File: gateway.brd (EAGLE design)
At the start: 100 x 146 mm, 25 parts, among them J1 RASPBERRYPI-40-PIN-GPIO_PTH_N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, Q1 BSS123

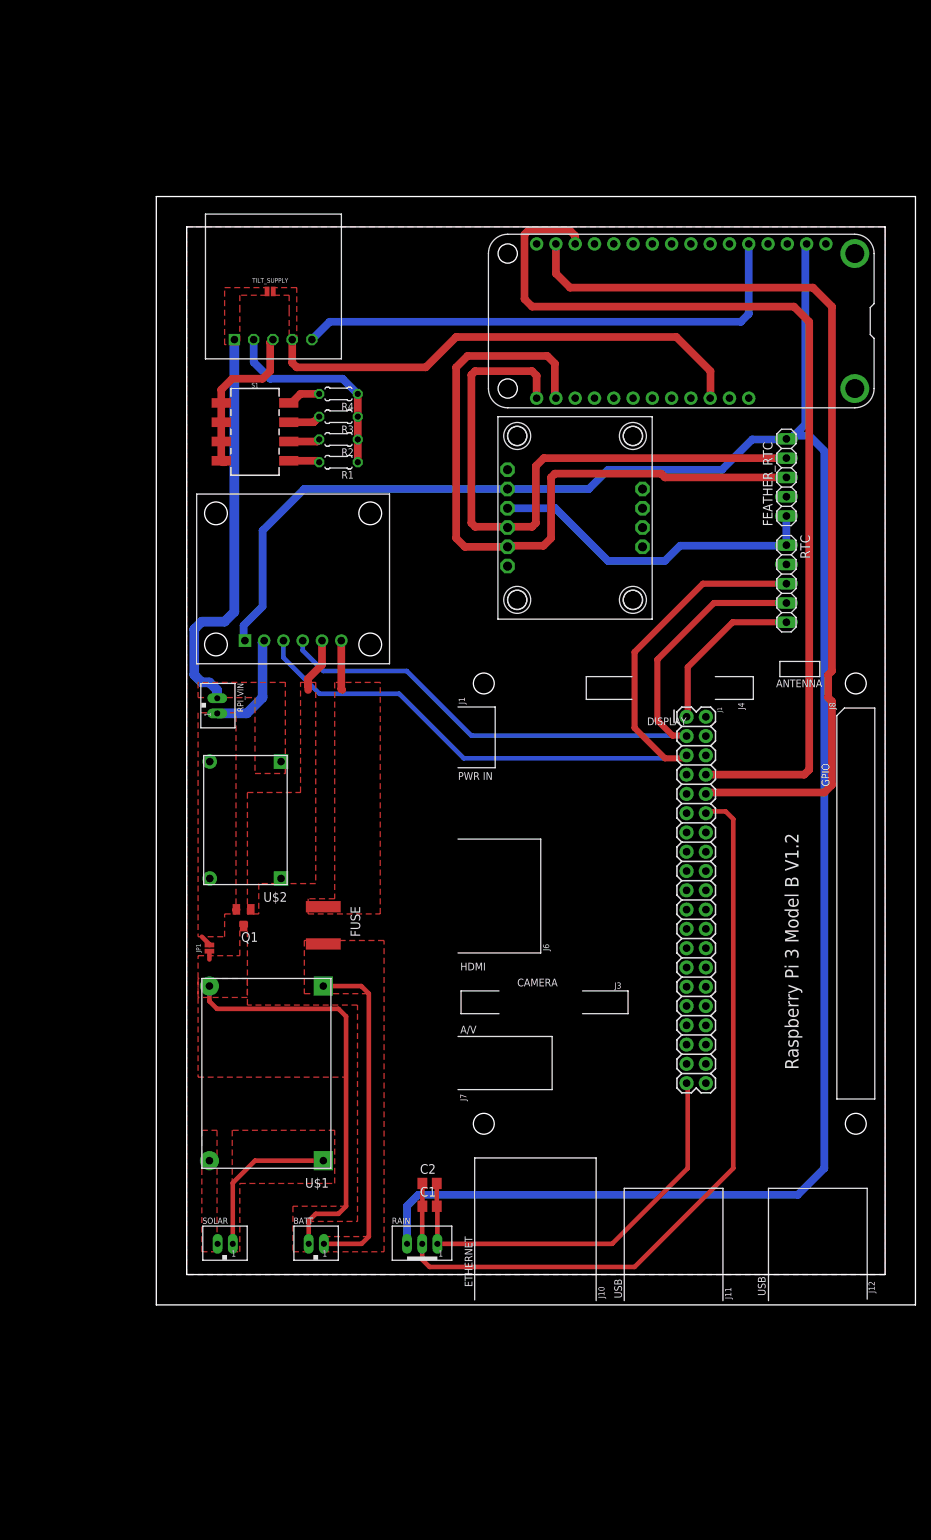
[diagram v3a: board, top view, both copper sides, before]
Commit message: added pads to the microcontrollers ( feather and pi )
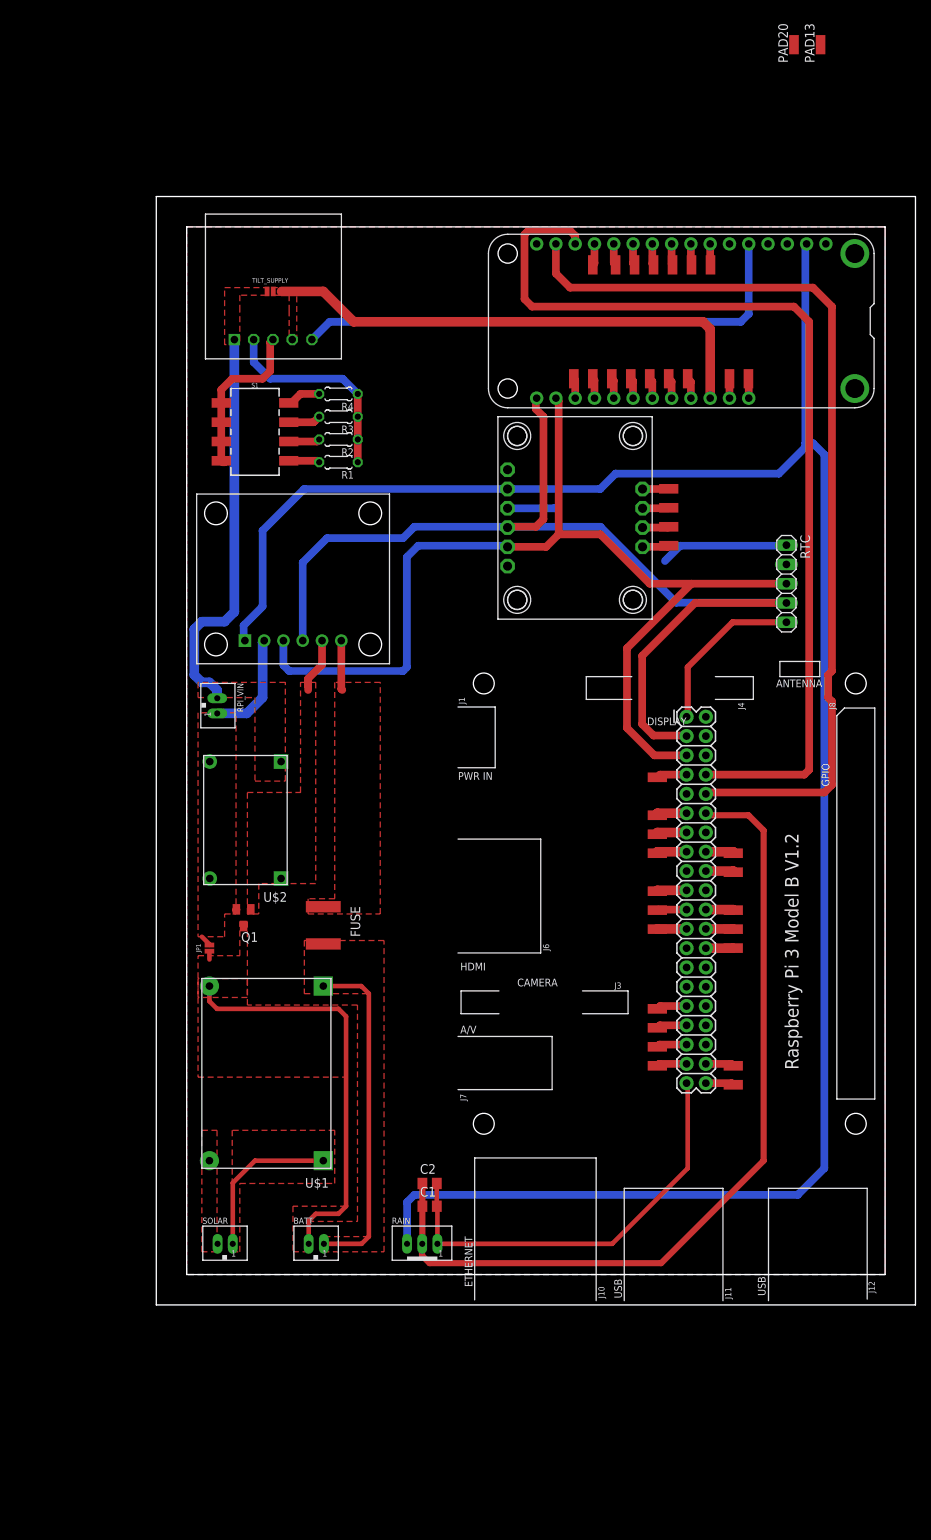
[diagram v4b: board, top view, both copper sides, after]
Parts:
- removed FEATHER_RTC: (no value), pinhead:1X05
- added PAD1, PAD10, PAD11, PAD12, PAD13, PAD14, PAD15, PAD16, PAD17, PAD18, PAD19, PAD2, PAD20, PAD21, PAD22, PAD23, PAD24, PAD25, PAD26, PAD27, PAD28, PAD29, PAD3, PAD30, PAD31, PAD32, PAD33, PAD34, PAD35, PAD36, PAD37, PAD38, PAD39, PAD4, PAD40, PAD5, PAD6, PAD7, PAD8, PAD9: WIREPADSMD1,27-254, wirepad:SMD1,27-2,54
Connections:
- removed net FEATHER_SCL: FEATHER_RTC.3, MS1.18, U$4.SCL
- removed net FEATHER_SDA: FEATHER_RTC.4, MS1.17, U$4.SDA
- new net AREF: PAD13.1
- new net CE0: J1.24, PAD4.1
- new net CE1: J1.26, PAD5.1
- new net EN: MS1.27, PAD29.1
- new net GP13: J1.33, PAD14.1
- new net GP17: J1.11, PAD7.1
- new net GP19: J1.35, PAD16.1
- new net GP20: J1.38, PAD17.1
- new net GP21: J1.40, PAD18.1
- new net GP22: J1.15, PAD8.1
- new net GP23: J1.16, PAD9.1
- new net GP24: J1.18, PAD10.1
- new net GP25: J1.22, PAD11.1
- new net GP26: J1.37, PAD19.1
- new net GP27: J1.13, PAD12.1
- new net GP4: J1.7, PAD6.1
- new net GP6: J1.31, PAD15.1
- new net GPIO10: MS1.22, PAD33.1
- new net GPIO11: MS1.23, PAD32.1
- new net GPIO12: MS1.24, PAD31.1
- new net GPIO13: MS1.25, PAD30.1
- new net GPIO5: MS1.19, PAD36.1
- new net GPIO6: MS1.20, PAD35.1
- new net GPIO9: MS1.21, PAD34.1
- new net GPIOA1: PAD20.1
- new net GPIOA2: MS1.7, PAD21.1
- new net GPIOA3: MS1.8, PAD22.1
- new net GPIOA4: MS1.9, PAD23.1
- new net GPIOA5: MS1.10, PAD24.1
- new net GPIOMISO: MS1.13, PAD26.1
- new net GPIOMOSI: MS1.12, PAD27.1
- new net GPIOSCK: MS1.11, PAD25.1
- new net MISO: J1.21, PAD2.1
- new net MOSI: J1.19, PAD3.1
- new net N$5: PAD38.1, U$4.ADR
- new net N$6: PAD39.1, U$4.PS0
- new net N$7: PAD40.1, U$4.PS1
- new net SCLK: J1.23, PAD1.1
- new net VBAT: MS1.28, PAD28.1
- net FEATHER_3.3V: no longer FEATHER_RTC.5
- net GND: no longer FEATHER_RTC.1
- net N$1: now also PAD37.1, U$4.INT; no longer MS1.27
- net RPI_SCL: now also MS1.18, U$4.SCL
- net RPI_SDA: now also MS1.17, U$4.SDA
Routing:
- net FEATHER_SCL: track 94.0 -> 0.00 mm
- net FEATHER_SDA: track 81.8 -> 0.00 mm
- net RPI_SDA: track 89.3 -> 139.6 mm, vias 0 -> 1
- net RPI_SCL: track 103.4 -> 138.5 mm
- net GND: track 144.2 -> 123.0 mm
- net RPI_GPIO18: track 106.9 -> 120.5 mm
- net GP17: track 0.00 -> 4.12 mm
- net GP27: track 0.00 -> 4.08 mm
- net GP22: track 0.00 -> 4.04 mm
- net GP6: track 0.00 -> 4.00 mm
- net GP4: track 0.00 -> 3.99 mm
- net GP13: track 0.00 -> 3.99 mm
- net GP19: track 0.00 -> 3.97 mm
- net MOSI: track 0.00 -> 3.96 mm
- net GP26: track 0.00 -> 3.95 mm
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
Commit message: added more fuse for more protection
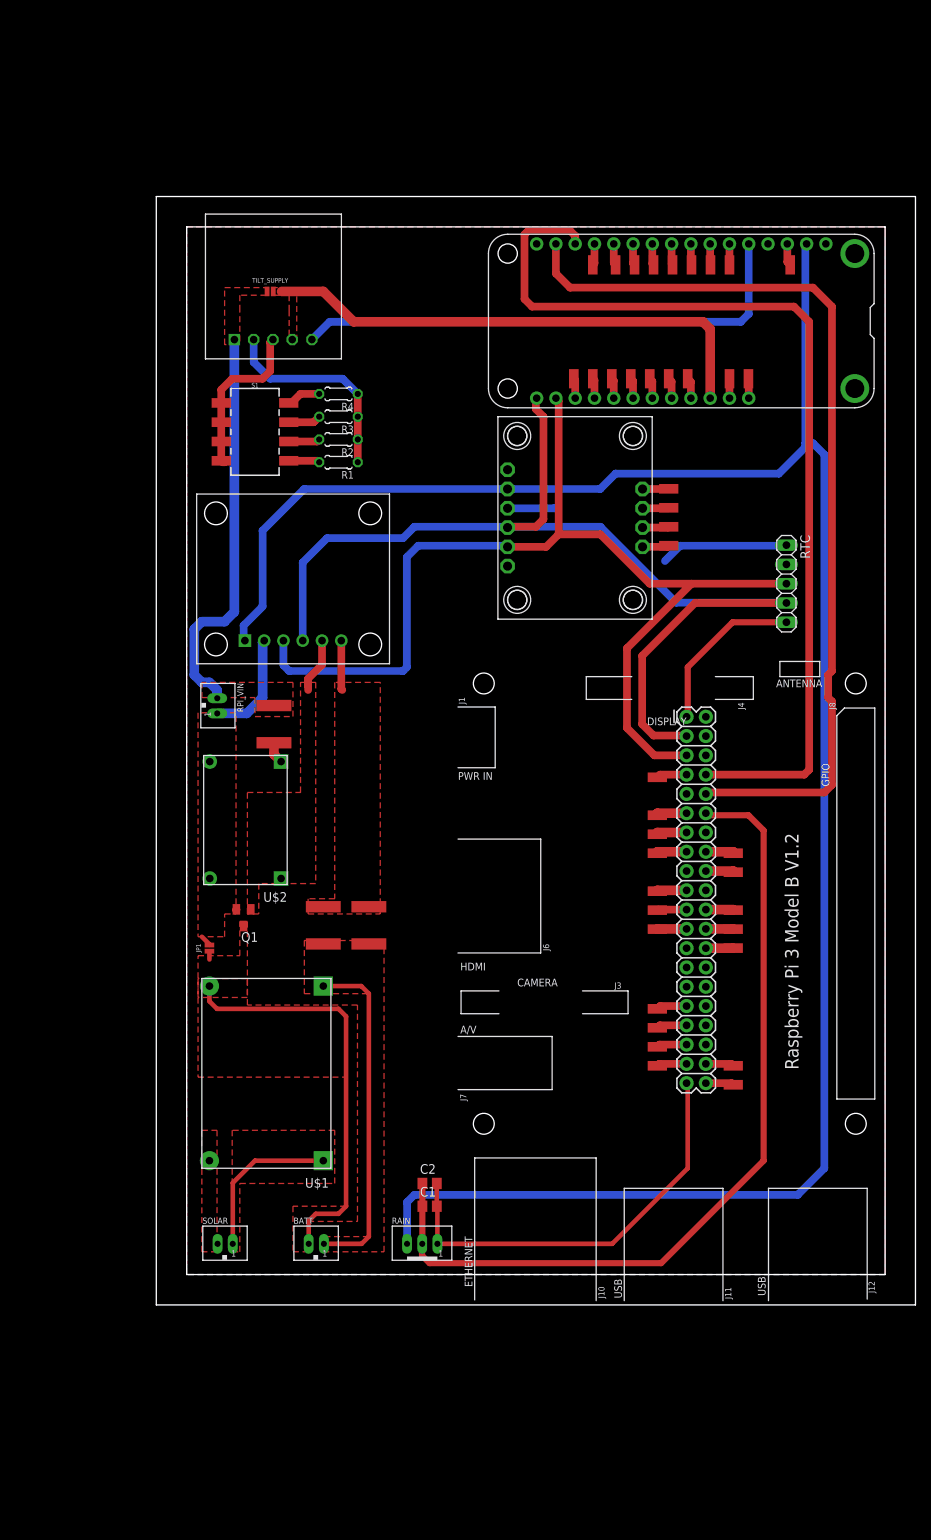
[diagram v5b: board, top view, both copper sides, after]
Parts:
- added FUSE1, FUSE2: MF-SMDF200, fuse:MF-SMDF050
- moved PAD20 30.2 mm to (75.5, 137.0)
- moved PAD13 29.3 mm to (83.5, 137.0)
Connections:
- new net N$8: FUSE2.1, U$2.OUT+
- net +5V: now also FUSE2.2; no longer U$2.OUT+
- net AREF: now also MS1.3
- net BATT+: now also FUSE1.1
- net GPIOA1: now also MS1.6
- net INA_VIN+: now also FUSE1.2
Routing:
- net AREF: track 0.00 -> 2.92 mm
- net N$8: track 0.00 -> 2.87 mm
- net GPIOA1: track 0.00 -> 2.76 mm
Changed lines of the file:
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@@
 <element name="MS1" library="adafruit" package="FEATHERWING_DIM" value="FEATHERWING_NODIM" x="94.55" y="141.03" rot="R180"/>
 <element name="RTC" library="pinhead" package="1X05" value="" x="83" y="95" rot="R270"/>
-<element name="FUSE" library="fuse" package="MF-SMDF050" value="MF-SMDF200" x="22" y="50" smashed="yes" rot="R90">
-<attribute name="NAME" x="25.59" y="52.51" size="1.27" layer="25" rot="R270"/>
-</element>
+<element name="FUSE" library="fuse" package="MF-SMDF050" value="MF-SMDF200" x="22" y="50" smashed="yes" rot="R90"/>
 <element name="Q1" library="transistor-small-signal" package="SOT23" value="BSS123" x="11.5" y="51" smashed="yes" rot="R180">
 <attribute name="NAME" x="13.405" y="49.095" size="1.27" layer="25" rot="R180"/>
@@
 <attribute name="NAME" x="5.857" y="47" size="0.6096" layer="25" font="vector" ratio="20" rot="R90" align="bottom-center"/>
 </element>
-<element name="U$2" library="edc_modules" package="MINI_360_BUCK" value="MINI_360_BUCK" x="17.24" y="72.37" rot="R180"/>
+<element name="U$2" library="edc_modules" package="MINI_360_BUCK" value="MINI_360_BUCK" x="17.24" y="72.37" smashed="yes" rot="R180">
+<attribute name="NAME" x="17.24" y="54.37" size="1.27" layer="25" rot="R180"/>
+<attribute name="VALUE" x="14.74" y="73.37" size="0.8128" layer="27" rot="R180"/>
+</element>
 <element name="RPI_VIN" library="SRG" package="JST_B2B-PH_HEADER" value="JST-PH_2-PIN_HEADER" x="7.98" y="78.99" rot="R270"/>
 <element name="RAIN" library="SRG" package="JST_B3B-PH_HEADER" value="JST-PH_3-PIN_HEADER" x="35" y="8"/>
@@
 <attribute name="VALUE" x="66" y="31.5" size="0.0254" layer="27" rot="R90"/>
 </element>
-<element name="PAD13" library="wirepad" package="SMD1,27-2,54" value="WIREPADSMD1,27-254" x="87.5" y="166"/>
-<element name="PAD20" library="wirepad" package="SMD1,27-2,54" value="WIREPADSMD1,27-254" x="84" y="166"/>
+<element name="PAD13" library="wirepad" package="SMD1,27-2,54" value="WIREPADSMD1,27-254" x="83.5" y="137" smashed="yes">
+<attribute name="VALUE" x="83.5" y="137" size="0.0254" layer="27"/>
+</element>
+<element name="PAD20" library="wirepad" package="SMD1,27-2,54" value="WIREPADSMD1,27-254" x="75.5" y="137" smashed="yes">
+<attribute name="VALUE" x="75.5" y="137" size="0.0254" layer="27"/>
+</element>
 <element name="PAD21" library="wirepad" package="SMD1,27-2,54" value="WIREPADSMD1,27-254" x="73" y="137" smashed="yes">
 <attribute name="VALUE" x="73" y="137" size="0.0254" layer="27"/>
@@
 <attribute name="VALUE" x="67.5" y="105" size="0.0254" layer="27" rot="R90"/>
 </element>
+<element name="FUSE1" library="fuse" package="MF-SMDF050" value="MF-SMDF200" x="28" y="50" smashed="yes" rot="R90"/>
+<element name="FUSE2" library="fuse" package="MF-SMDF050" value="MF-SMDF200" x="15.5" y="76.5" smashed="yes" rot="R90"/>
 </elements>
 <signals>
@@
 <vertex x="30" y="48"/>
 </polygon>
+<contactref element="FUSE1" pad="1"/>
 </signal>
 <signal name="BATT-">
@@
 </signal>
 <signal name="+5V">
-<contactref element="U$2" pad="OUT+"/>
 <contactref element="RPI_VIN" pad="P2"/>
 <contactref element="U$3" pad="VDD"/>
-<polygon width="0.6096" layer="1">
-<vertex x="5.5" y="82"/>
-<vertex x="5.5" y="80"/>
+<polygon width="0.6096" layer="1" thermals="no">
+<vertex x="6" y="82"/>
+<vertex x="6" y="80"/>
 <vertex x="13" y="80"/>
-<vertex x="13" y="69"/>
-<vertex x="17" y="69"/>
-<vertex x="17" y="82"/>
+<vertex x="13" y="77.5"/>
+<vertex x="18" y="77.5"/>
+<vertex x="18" y="82"/>
 </polygon>
 <wire x1="10.286" y1="127.159" x2="10.286" y2="91.286" width="1.27" layer="16"/>
@@
 <vertex x="11" y="126.5"/>
 </polygon>
+<contactref element="FUSE2" pad="2"/>
 </signal>
 <signal name="INA_VIN-">
@@
 <wire x1="24.37" y1="87.504" x2="24.37" y2="81.13" width="1.016" layer="1"/>
 <wire x1="24.37" y1="81.13" x2="24.5" y2="81" width="1.016" layer="1"/>
+<contactref element="FUSE1" pad="2"/>
 </signal>
 <signal name="3.3V">
@@
 <signal name="GPIOA1">
 <contactref element="PAD20" pad="1"/>
+<contactref element="MS1" pad="6"/>
+<wire x1="75.5" y1="139.76" x2="75.5" y2="137" width="1.016" layer="1"/>
 </signal>
 <signal name="AREF">
 <contactref element="PAD13" pad="1"/>
+<contactref element="MS1" pad="3"/>
+<wire x1="83.12" y1="139.76" x2="83.12" y2="137.38" width="1.016" layer="1"/>
+<wire x1="83.12" y1="137.38" x2="83.5" y2="137" width="1.016" layer="1"/>
 </signal>
 <signal name="VBAT">
@@
 <wire x1="67.435" y1="104.935" x2="67.5" y2="105" width="1.016" layer="1"/>
 </signal>
+<signal name="N$8">
+<contactref element="U$2" pad="OUT+"/>
+<contactref element="FUSE2" pad="1"/>
+<wire x1="15.5" y1="74.05" x2="15.5" y2="72.51" width="1.27" layer="1"/>
+<wire x1="15.5" y1="72.51" x2="16.44" y2="71.57" width="1.27" layer="1"/>
+</signal>
 </signals>

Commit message: added a 2mm tplace line around board.
changed rain header to 1.5mm pitch
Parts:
- added C3, C4: (no value), rcl:C1812
- RAIN: value JST-PH_3-PIN_HEADER -> B3B-ZR; device SRG:JST_B3B-PH_HEADER -> jst:B3B-ZR
- moved BATT 25.7 mm to (27.0, 33.0)
- moved S1 23.9 mm to (36.5, 119.5), turned to 180 degrees
- moved SOLAR 21.6 mm to (27.0, 20.0)
- moved R4 19.0 mm to (40.5, 110.5), turned to 90 degrees
- moved R3 15.4 mm to (38.0, 110.5), turned to 90 degrees
- moved INA219 15.0 mm to (17.0, 99.5)
- moved RAIN 12.5 mm to (35.0, 20.5), turned to 180 degrees
- moved R2 11.5 mm to (35.0, 110.5), turned to 90 degrees
- moved R1 8.51 mm to (32.5, 110.5), turned to 90 degrees
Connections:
- net +5V: now also C3.1, C4.1
- net FEATHER_3.3V: now also RAIN.3; no longer RAIN.P3
- net GND: now also C3.2, C4.2, RAIN.1; no longer RAIN.P1
- net RPI_GPIO18: now also RAIN.2; no longer RAIN.P2
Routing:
- net GND: track 123.0 -> 201.3 mm
- net BATT-: track 55.7 -> 1.09 mm
- net BATT+: track 44.7 -> 0.00 mm
- net SOLAR+: track 21.2 -> 0.00 mm
- net +5V: track 53.0 -> 71.1 mm
- net INA_VIN+: track 6.56 -> 23.5 mm
- net INA_VIN-: track 7.26 -> 21.8 mm
- net FEATHER_3.3V: track 277.9 -> 267.4 mm
- net RPI_SCL: track 138.5 -> 129.1 mm
- net RPI_SDA: track 139.6 -> 133.1 mm, vias 1 -> 0
- net DELAY: track 22.0 -> 28.4 mm
- net N$12: track 4.51 -> 2.20 mm
- net N$11: track 4.32 -> 2.24 mm
- net N$9: track 4.09 -> 2.20 mm
- net N$10: track 4.13 -> 2.24 mm

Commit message: forgot to commit brd files
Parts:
- moved S1 10.5 mm to (36.5, 130.0)
- moved R4 8.51 mm to (40.0, 119.0), turned to 180 degrees
- moved R1 7.57 mm to (40.0, 111.5), turned to 180 degrees
- moved R3 6.32 mm to (40.0, 116.5), turned to 180 degrees
- moved R2 6.10 mm to (40.0, 114.0), turned to 180 degrees
- moved INA219 4.53 mm to (21.5, 100.0)
- moved PAD37 2.00 mm to (67.5, 100.5)
- moved PAD38 2.00 mm to (67.5, 98.0)
- moved PAD39 2.00 mm to (67.5, 105.5)
- moved PAD40 2.00 mm to (67.5, 103.0)
- moved U$4 2.00 mm to (45.0, 115.0)
- moved MS1 1.50 mm to (94.5, 139.5)
- moved PAD13 1.50 mm to (83.5, 135.5)
- moved PAD20 1.50 mm to (75.5, 135.5)
- moved PAD21 1.50 mm to (73.0, 135.5)
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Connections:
- net +3V3: no longer RTC.5
- net FEATHER_3.3V: now also RTC.5
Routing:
- net GND: track 201.3 -> 232.2 mm
- net N$9: track 2.20 -> 28.0 mm
- net N$10: track 2.24 -> 24.2 mm
- net RPI_SDA: track 133.1 -> 123.4 mm
- net N$11: track 2.24 -> 11.4 mm
- net RPI_TX: track 128.4 -> 136.5 mm
- net +3V3: track 22.0 -> 15.0 mm
- net N$12: track 2.20 -> 9.22 mm
- net INA_VIN-: track 21.8 -> 24.7 mm
- net RPI_RX: track 122.6 -> 120.2 mm
- net VBAT: track 2.58 -> 4.08 mm
- net GPIO6: track 2.65 -> 4.15 mm
- net GPIO9: track 2.67 -> 4.17 mm
- net GPIO5: track 2.63 -> 4.13 mm
- net GPIO13: track 2.73 -> 4.23 mm
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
